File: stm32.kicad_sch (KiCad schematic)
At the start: 29 parts, among them J13 Screw_Terminal_01x04, U22 REF3030, U23 STM32H743VITx, Y4 8Mhz

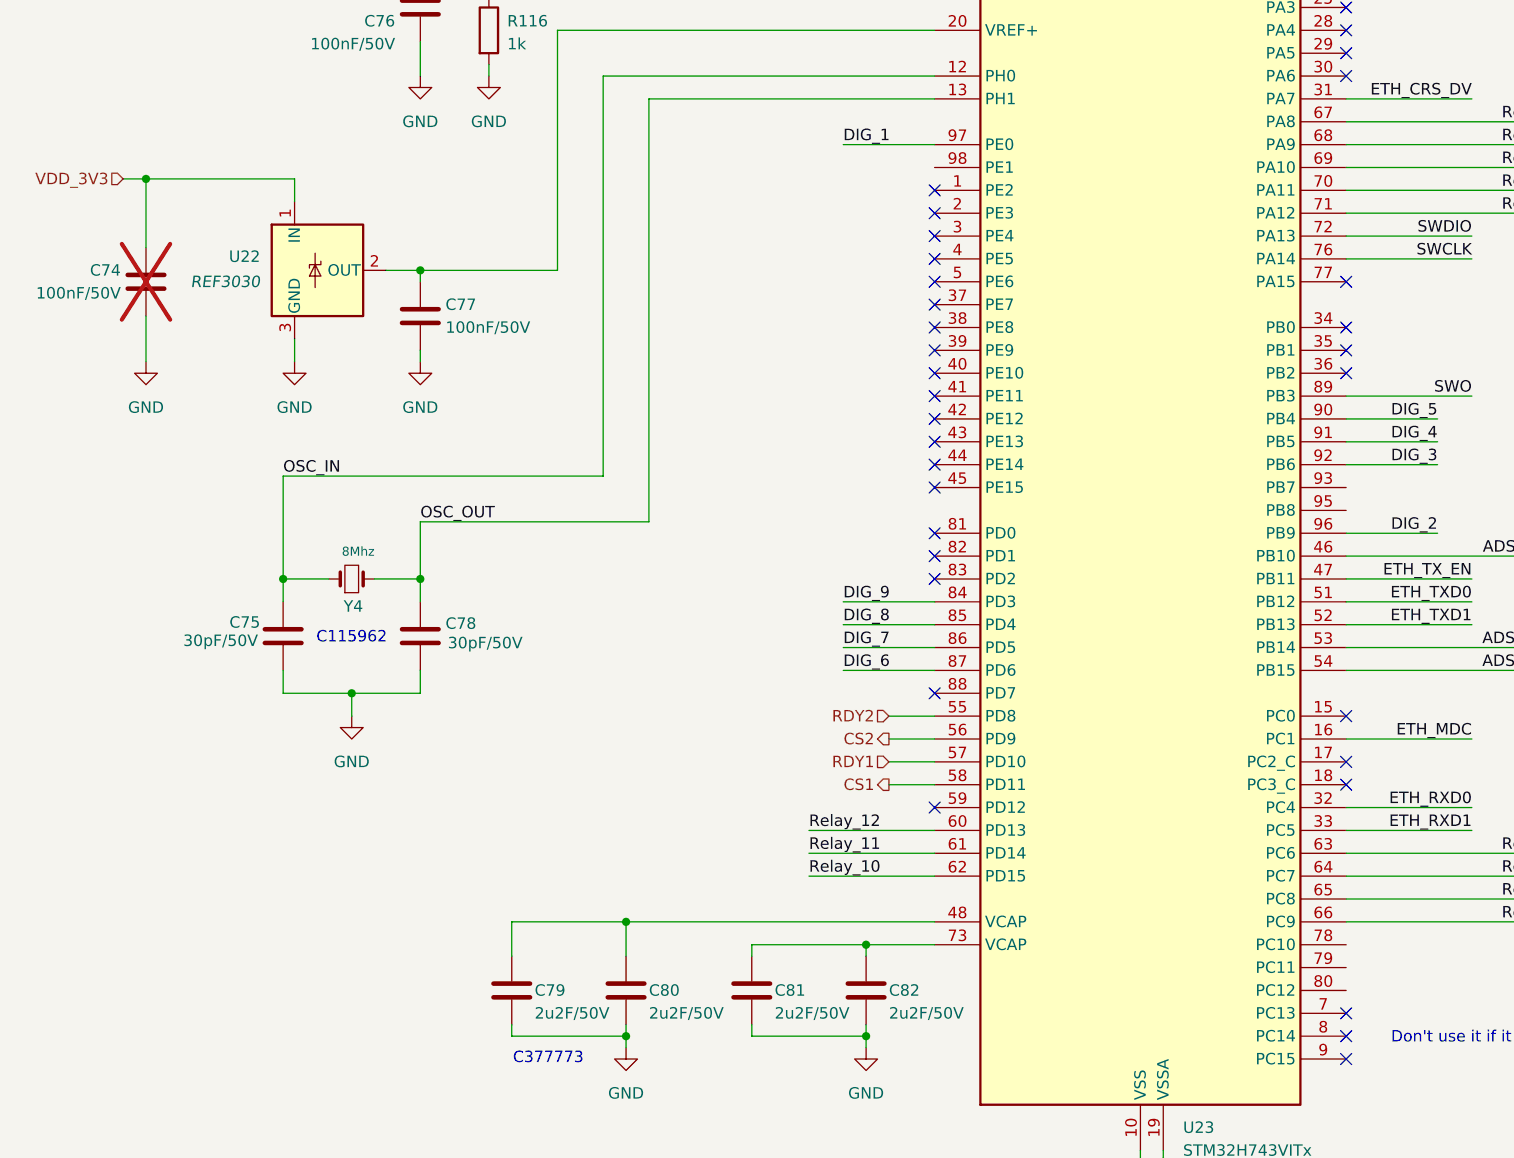
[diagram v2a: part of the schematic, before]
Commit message: Se traza vcc, digital, analog, relay, esta por terminar corregir GND y revisar nuevamente
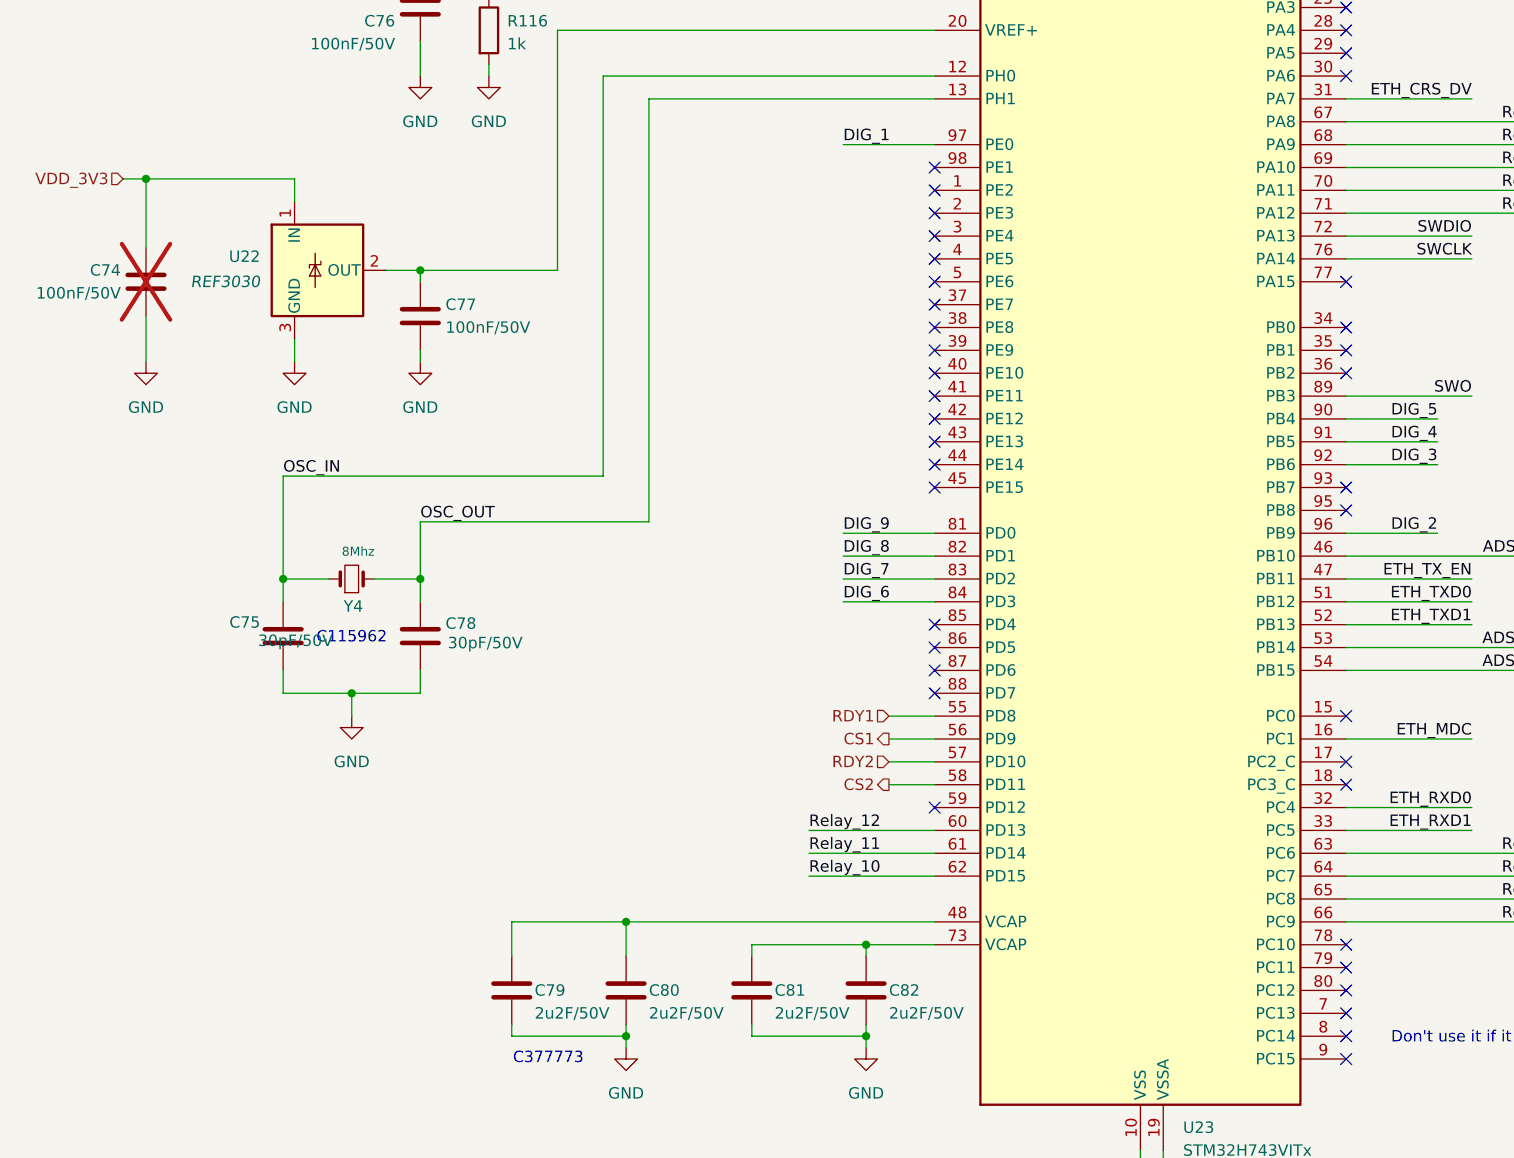
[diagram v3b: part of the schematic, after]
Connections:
- net CS1: now also U23.56 (PD9); no longer U23.58 (PD11)
- net CS2: now also U23.58 (PD11); no longer U23.56 (PD9)
- net DIG_6: now also U23.84 (PD3); no longer U23.87 (PD6)
- net DIG_7: now also U23.83 (PD2); no longer U23.86 (PD5)
- net DIG_8: now also U23.82 (PD1); no longer U23.85 (PD4)
- net DIG_9: now also U23.81 (PD0); no longer U23.84 (PD3)
- net RDY1: now also U23.55 (PD8); no longer U23.57 (PD10)
- net RDY2: now also U23.57 (PD10); no longer U23.55 (PD8)
- no-connect marks 34 -> 40
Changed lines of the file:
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@@
 	)
 	(no_connect
-		(at 182.88 123.19)
-	)
-	(no_connect
 		(at 182.88 151.13)
 	)
@@
 	)
 	(no_connect
+		(at 182.88 133.35)
+	)
+	(no_connect
+		(at 228.6 166.37)
+	)
+	(no_connect
 		(at 228.6 140.97)
 	)
 	(no_connect
+		(at 182.88 130.81)
+	)
+	(no_connect
 		(at 228.6 102.87)
 	)
@@
 	)
 	(no_connect
+		(at 228.6 168.91)
+	)
+	(no_connect
 		(at 182.88 82.55)
 	)
@@
 	)
 	(no_connect
+		(at 182.88 80.01)
+	)
+	(no_connect
 		(at 182.88 105.41)
 	)
@@
 	)
 	(no_connect
+		(at 182.88 135.89)
+	)
+	(no_connect
 		(at 182.88 92.71)
 	)
@@
 	)
 	(no_connect
+		(at 228.6 118.11)
+	)
+	(no_connect
 		(at 228.6 54.61)
 	)
@@
 	)
 	(no_connect
+		(at 228.6 171.45)
+	)
+	(no_connect
 		(at 228.6 64.77)
 	)
@@
 	)
 	(no_connect
-		(at 182.88 125.73)
+		(at 228.6 115.57)
 	)
 	(no_connect
@@
 	)
 	(no_connect
-		(at 182.88 120.65)
-	)
-	(no_connect
 		(at 228.6 176.53)
 	)
@@
 	(wire
 		(pts
+			(xy 172.72 123.19) (xy 182.88 123.19)
+		)
+		(stroke
+			(width 0)
+			(type default)
+		)
+	)
+	(wire
+		(pts
 			(xy 231.14 33.02) (xy 247.65 33.02)
 		)
@@
 		)
 	)
-	(wire
-		(pts
-			(xy 172.72 130.81) (xy 182.88 130.81)
-		)
-		(stroke
-			(width 0)
-			(type default)
-		)
-	)
 	(bus
 		(pts
@@
 	(wire
 		(pts
-			(xy 172.72 128.27) (xy 182.88 128.27)
-		)
-		(stroke
-			(width 0)
-			(type default)
-		)
-	)
-	(wire
-		(pts
 			(xy 22.86 81.28) (xy 31.75 81.28)
 		)
@@
 		)
 	)
+	(wire
+		(pts
+			(xy 172.72 128.27) (xy 182.88 128.27)
+		)
+		(stroke
+			(width 0)
+			(type default)
+		)
+	)
 	(bus
 		(pts
@@
 	(wire
 		(pts
+			(xy 172.72 125.73) (xy 182.88 125.73)
+		)
+		(stroke
+			(width 0)
+			(type default)
+		)
+	)
+	(wire
+		(pts
 			(xy 118.11 138.43) (xy 118.11 140.97)
 		)
@@
 		)
 	)
+	(wire
+		(pts
+			(xy 172.72 120.65) (xy 182.88 120.65)
+		)
+		(stroke
+			(width 0)
+			(type default)
+		)
+	)
 	(bus
 		(pts
@@
 	(wire
 		(pts
-			(xy 172.72 133.35) (xy 182.88 133.35)
-		)
-		(stroke
-			(width 0)
-			(type default)
-		)
-	)
-	(wire
-		(pts
 			(xy 22.86 86.36) (xy 31.75 86.36)
 		)
@@
 	(wire
 		(pts
-			(xy 182.88 135.89) (xy 172.72 135.89)
-		)
-		(stroke
-			(width 0)
-			(type default)
-		)
-	)
-	(wire
-		(pts
 			(xy 228.6 87.63) (xy 242.57 87.63)
 		)
@@
 	)
 	(label "DIG_6"
-		(at 172.72 135.89 0)
+		(at 172.72 128.27 0)
 		(effects
 			(font
@@
 	)
 	(label "DIG_8"
-		(at 172.72 130.81 0)
+		(at 172.72 123.19 0)
 		(effects
 			(font
@@
 	)
 	(label "DIG_7"
-		(at 172.72 133.35 0)
+		(at 172.72 125.73 0)
 		(effects
 			(font
@@
 	)
 	(label "DIG_9"
-		(at 172.72 128.27 0)
+		(at 172.72 120.65 0)
 		(effects
 			(font
@@
 		)
 	)
+	(hierarchical_label "RDY1"
+		(shape input)
+		(at 177.8 140.97 180)
+		(effects
+			(font
+				(size 1.27 1.27)
+			)
+			(justify right)
+		)
+	)
 	(hierarchical_label "{RELAY}"
 		(shape output)
@@
 	(hierarchical_label "CS1"
 		(shape output)
-		(at 177.8 148.59 180)
+		(at 177.8 143.51 180)
 		(effects
 			(font
@@
 		)
 	)
-	(hierarchical_label "RDY1"
-		(shape input)
-		(at 177.8 146.05 180)
-		(effects
-			(font
-				(size 1.27 1.27)
-			)
-			(justify right)
-		)
-	)
 	(hierarchical_label "RDY2"
 		(shape input)
-		(at 177.8 140.97 180)
+		(at 177.8 146.05 180)
 		(effects
 			(font
@@
 		)
 	)
-	(hierarchical_label "CS2"
-		(shape output)
-		(at 177.8 143.51 180)
+	(hierarchical_label "{ETH}"
+		(shape bidirectional)
+		(at 50.8 110.49 0)
 		(effects
 			(font
 				(size 1.27 1.27)
 			)
-			(justify right)
+			(justify left)
 		)
 	)
-	(hierarchical_label "{ETH}"
-		(shape bidirectional)
-		(at 50.8 110.49 0)
+	(hierarchical_label "CS2"
+		(shape output)
+		(at 177.8 148.59 180)
 		(effects
 			(font
 				(size 1.27 1.27)
 			)
-			(justify left)
+			(justify right)
 		)
 	)
@@
 					(size 1.27 1.27)
 				)
-				(justify right)
+				(justify left)
 			)
 		)

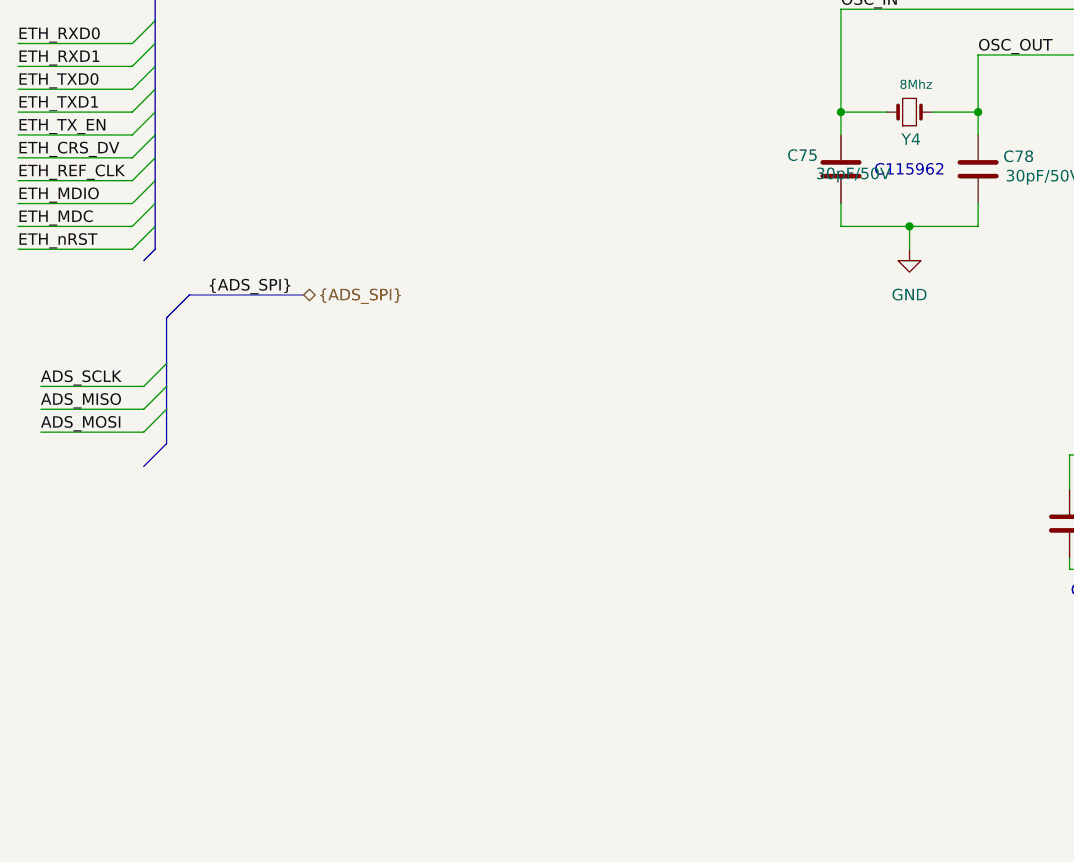
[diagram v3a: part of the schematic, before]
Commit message: Se termina de revisar la placa. Se corrige la terminación de los transformadores internos del puerto ethernet. Se revisa GND, espaciado, añadimos notas. Falta enlazar las partes de JLCPCN
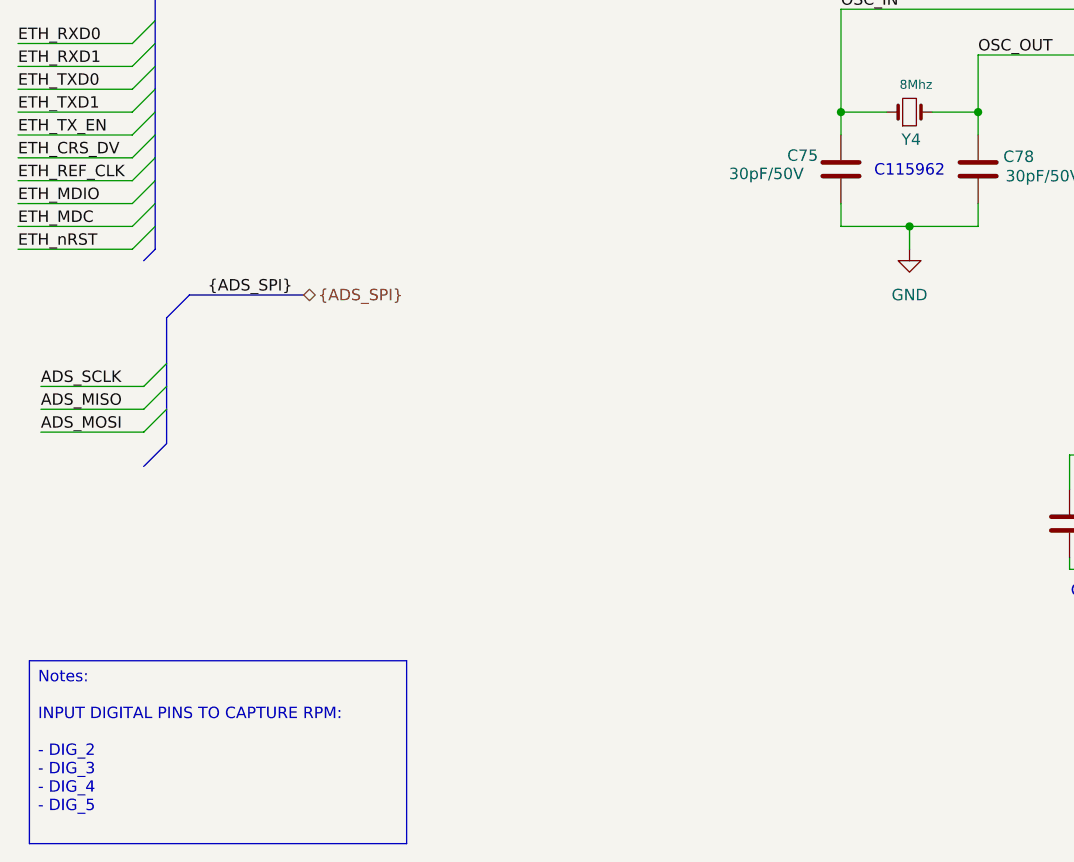
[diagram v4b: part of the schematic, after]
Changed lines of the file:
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@@
 		)
 	)
+	(text_box "Notes:\n\nINPUT DIGITAL PINS TO CAPTURE RPM:\n\n- DIG_2\n- DIG_3\n- DIG_4\n- DIG_5"
+		(exclude_from_sim no)
+		(at 20.32 186.69 0)
+		(size 41.91 20.32)
+		(margins 0.9525 0.9525 0.9525 0.9525)
+		(stroke
+			(width 0)
+			(type solid)
+		)
+		(fill
+			(type none)
+		)
+		(effects
+			(font
+				(size 1.27 1.27)
+			)
+			(justify left top)
+		)
+	)
 	(junction
 		(at 283.21 53.34)
@@
 		)
 		(property "Value" "30pF/50V"
-			(at 107.696 132.588 0)
+			(at 98.044 132.588 0)
 			(effects
 				(font
